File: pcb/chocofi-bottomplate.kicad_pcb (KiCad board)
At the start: 2 copper layers, 111.4 x 90 mm, 7 parts

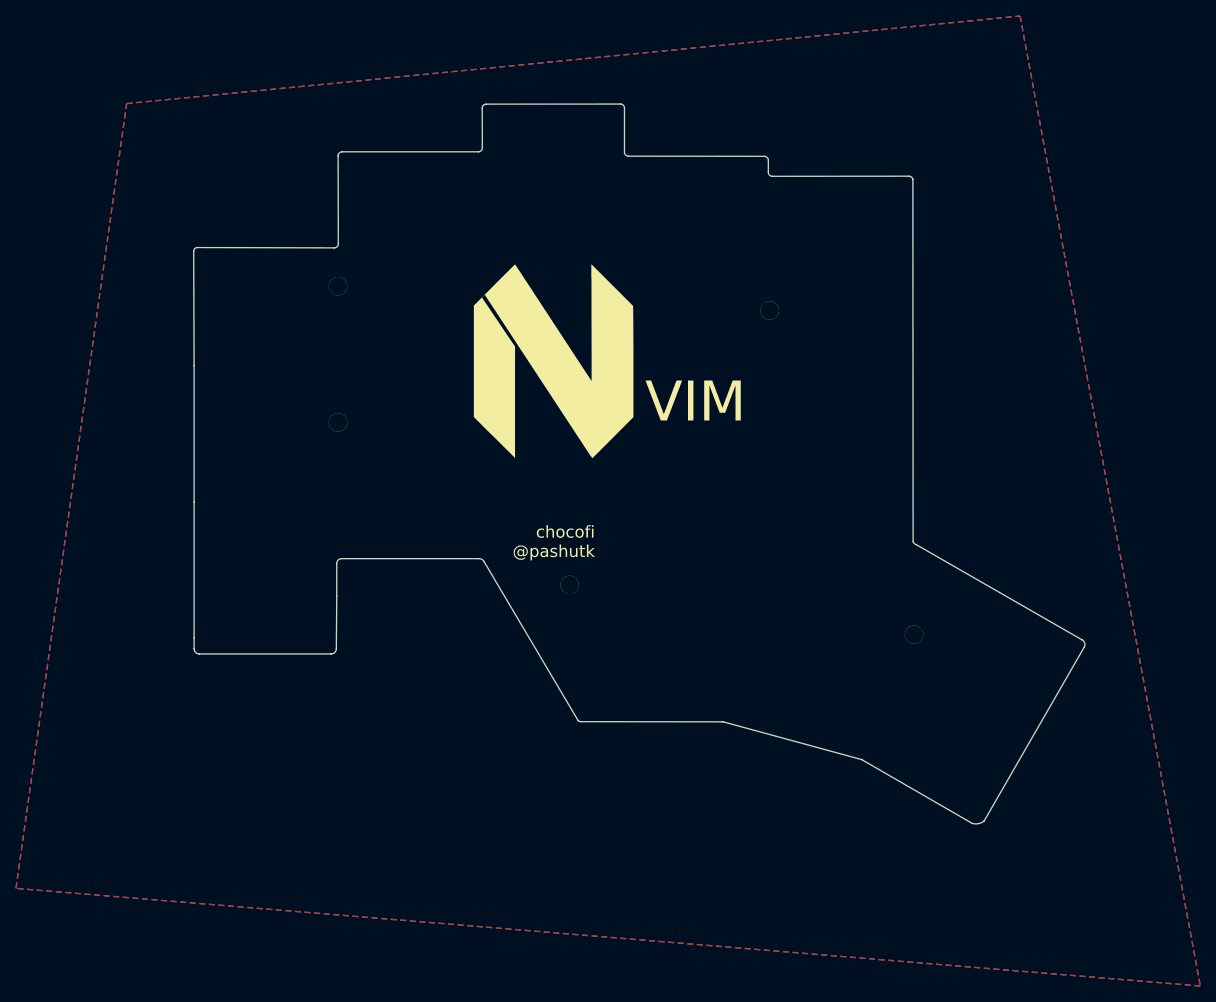
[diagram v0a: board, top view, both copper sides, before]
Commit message: fix: bottom plate not don't cover entire pcb
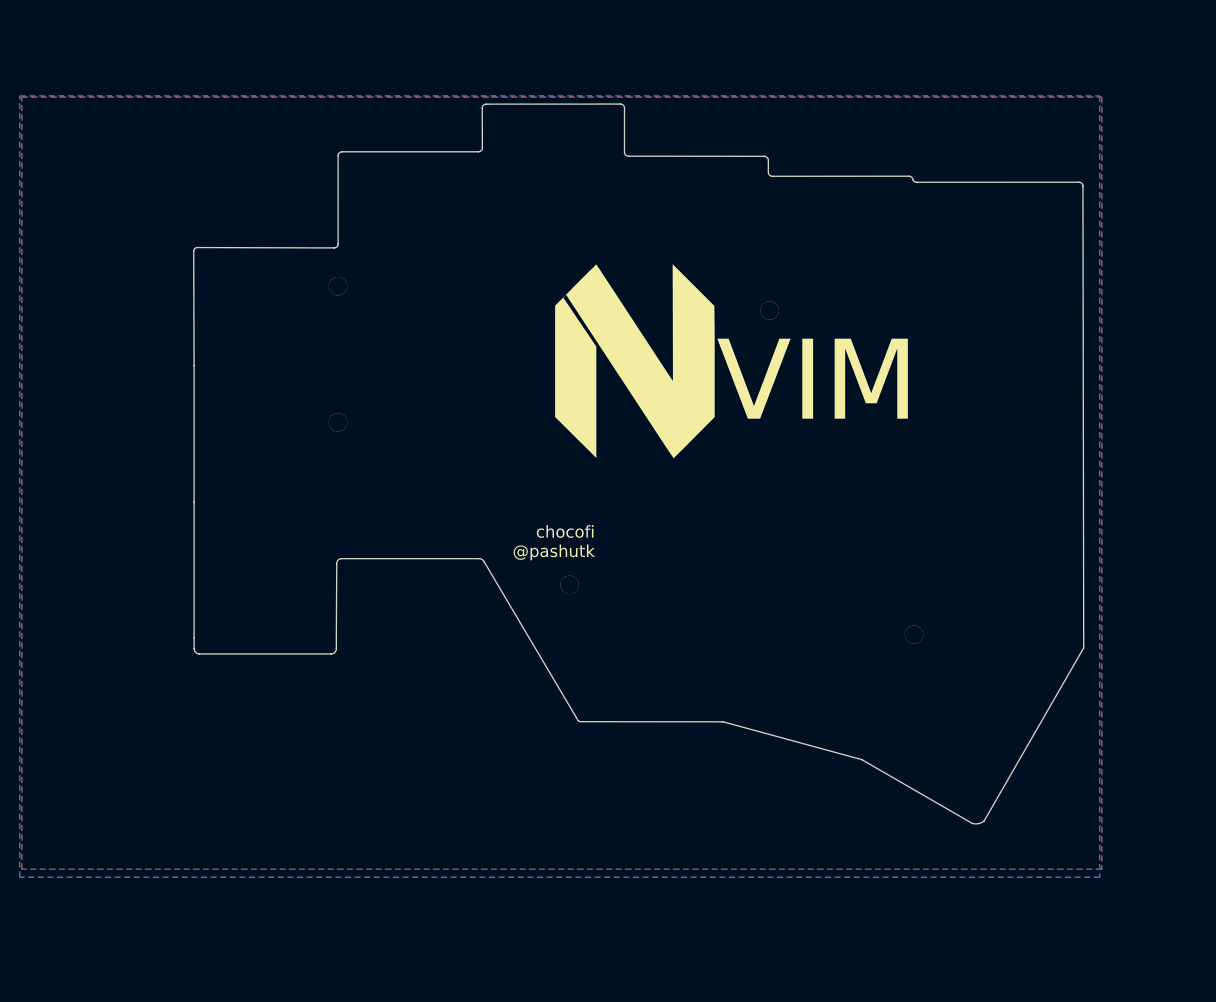
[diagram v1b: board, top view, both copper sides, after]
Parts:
- removed the G*** at (121.9, 76.2) (x2)
- removed h3: h3, kbd:M2_Threads_v2
- removed h4: h4, kbd:M2_Threads_v2
- removed h5: h5, kbd:M2_Threads_v2
- removed h6: h6, kbd:M2_Threads_v2
- removed h7: h7, kbd:M2_Threads_v2
- added ?: , , F.Cu at (165.1, 71.1)
- added ?: , , F.Cu at (95.0, 66.8)
- added ?: , , F.Cu at (94.0, 81.3)
- added ?: , , F.Cu at (129.5, 101.6)
- added ?: , , F.Cu at (172.7, 111.8)
- added G***: LOGO, LOGO, F.Cu at (132.1, 76.2)
- added G***: LOGO, LOGO, B.Cu at (132.1, 76.2)
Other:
- board size 111.4 x 90 mm -> 111.3 x 90 mm

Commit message: chore: update bottom plate
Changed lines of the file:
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@@
   (footprint "" (layer "F.Cu")
     (at 165.1 71.12)
-    (fp_text reference "" (at 0 0) (layer "F.SilkS")
-      (effects (font (size 1.27 1.27) (thickness 0.15)))
-    )
-    (fp_text value "" (at 0 0) (layer "F.SilkS")
-      (effects (font (size 1.27 1.27) (thickness 0.15)))
+    (fp_text reference "" (at 0 0) (layer "F.SilkS") hide
+      (effects (font (size 1 1) (thickness 0.15)))
+    )
+    (fp_text value "" (at 0 0) (layer "F.SilkS") hide
+      (effects (font (size 1 1) (thickness 0.15)))
     )
     (pad "" thru_hole circle (at -16.129 -1.27) (size 2.3 2.3) (drill 2.3) (layers *.Cu *.Mask))
@@
   (footprint "" (layer "F.Cu")
     (at 95 66.802)
-    (fp_text reference "" (at 0 0) (layer "F.SilkS")
-      (effects (font (size 1.27 1.27) (thickness 0.15)))
-    )
-    (fp_text value "" (at 0 0) (layer "F.SilkS")
-      (effects (font (size 1.27 1.27) (thickness 0.15)))
+    (fp_text reference "" (at 0 0) (layer "F.SilkS") hide
+      (effects (font (size 1 1) (thickness 0.15)))
+    )
+    (fp_text value "" (at 0 0) (layer "F.SilkS") hide
+      (effects (font (size 1 1) (thickness 0.15)))
     )
     (pad "" thru_hole circle (at 0 0) (size 2.3 2.3) (drill 2.3) (layers *.Cu *.Mask))
@@
   (footprint "" (layer "F.Cu")
     (at 93.98 81.28)
-    (fp_text reference "" (at 0 0) (layer "F.SilkS")
-      (effects (font (size 1.27 1.27) (thickness 0.15)))
-    )
-    (fp_text value "" (at 0 0) (layer "F.SilkS")
-      (effects (font (size 1.27 1.27) (thickness 0.15)))
+    (fp_text reference "" (at 0 0) (layer "F.SilkS") hide
+      (effects (font (size 1 1) (thickness 0.15)))
+    )
+    (fp_text value "" (at 0 0) (layer "F.SilkS") hide
+      (effects (font (size 1 1) (thickness 0.15)))
     )
     (pad "" thru_hole circle (at 1.02 2.54) (size 2.3 2.3) (drill 2.3) (layers *.Cu *.Mask))
@@
   (footprint "" (layer "F.Cu")
     (at 129.54 101.6)
-    (fp_text reference "" (at 0 0) (layer "F.SilkS")
-      (effects (font (size 1.27 1.27) (thickness 0.15)))
-    )
-    (fp_text value "" (at 0 0) (layer "F.SilkS")
-      (effects (font (size 1.27 1.27) (thickness 0.15)))
+    (fp_text reference "" (at 0 0) (layer "F.SilkS") hide
+      (effects (font (size 1 1) (thickness 0.15)))
+    )
+    (fp_text value "" (at 0 0) (layer "F.SilkS") hide
+      (effects (font (size 1 1) (thickness 0.15)))
     )
     (pad "" thru_hole circle (at -5.588 2.54) (size 2.3 2.3) (drill 2.3) (layers *.Cu *.Mask))
@@
   (footprint "" (layer "F.Cu")
     (at 172.72 111.76)
-    (fp_text reference "" (at 0 0) (layer "F.SilkS")
-      (effects (font (size 1.27 1.27) (thickness 0.15)))
-    )
-    (fp_text value "" (at 0 0) (layer "F.SilkS")
-      (effects (font (size 1.27 1.27) (thickness 0.15)))
+    (fp_text reference "" (at 0 0) (layer "F.SilkS") hide
+      (effects (font (size 1 1) (thickness 0.15)))
+    )
+    (fp_text value "" (at 0 0) (layer "F.SilkS") hide
+      (effects (font (size 1 1) (thickness 0.15)))
     )
     (pad "" thru_hole circle (at -5.715 -1.397) (size 2.3 2.3) (drill 2.3) (layers *.Cu *.Mask))
@@
       )
     )
-  )
-  (zone (net 0) (net_name "") (layer "B.Cu") (hatch edge 0.508)
-    (connect_pads (clearance 0.508))
-    (min_thickness 0.254) (filled_areas_thickness no)
-    (fill yes (thermal_gap 0.508) (thermal_bridge_width 0.508))
-    (polygon
-      (pts
-        (xy 190.22 140.68651)
-        (xy 55.22 140.68651)
-        (xy 55.22 43.01951)
-        (xy 190.22 43.01951)
-      )
-    )
